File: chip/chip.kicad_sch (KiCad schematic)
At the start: 2 parts, among them J1 DF40TC-30DP-0.4V(51), U1 HOME_VFBGA67_INTERFACE

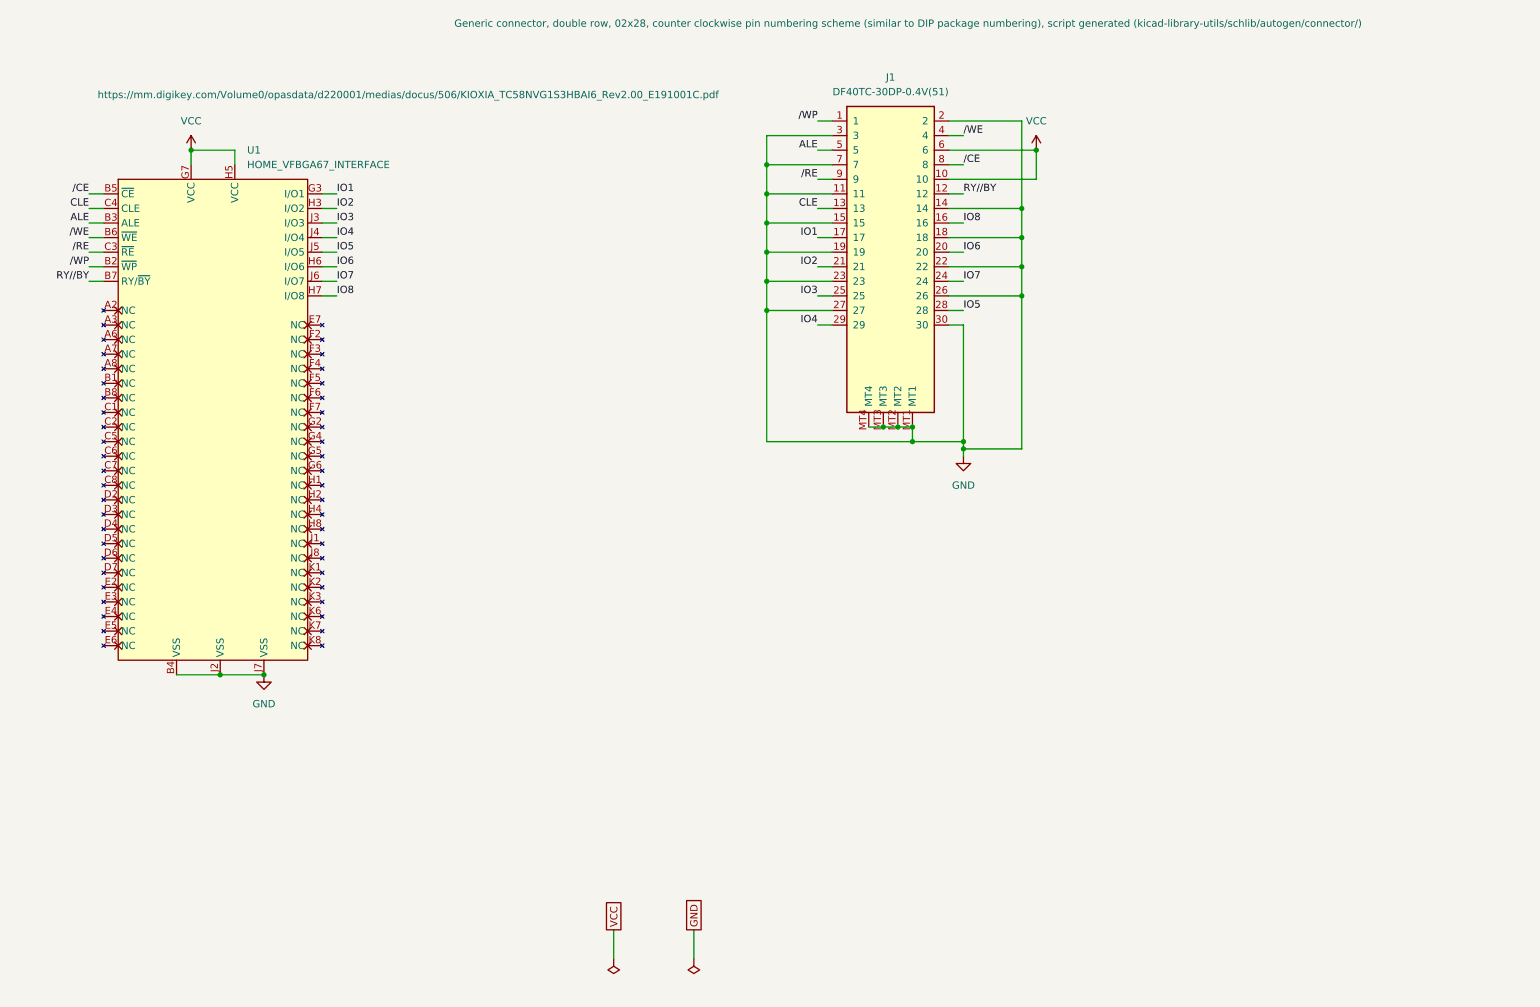
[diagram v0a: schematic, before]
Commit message: Draw board C's schematic: real NAND, DF40 receptacle, decoupling
U1 keeps the TC58NVG1S3HBAI6 symbol and every net label, but takes the
non-mirrored BGA-67 footprint and its real part number as Value. J1 swaps the
DF40 plug symbol for the 4.0 mm receptacle.

The swap is safe because the two symbols are pin-identical: 30 pins, same
numbers, same positions, same orientations, verified before the edit. So every
wire endpoint stays on the same pin number and no net moves. The plug/receptacle
difference lives entirely in the footprint, which is where the face-to-face
mirror belongs.

Adds C1 100nF and C2 1uF across VCC/GND. The target board's decoupling is now
two boards and a mated connector away from the die.

ERC clean. check_mating confirms board C's ball-to-net map is still identical
to carrier A's.

Co-Authored-By: Claude Opus 5 <noreply@anthropic.com>
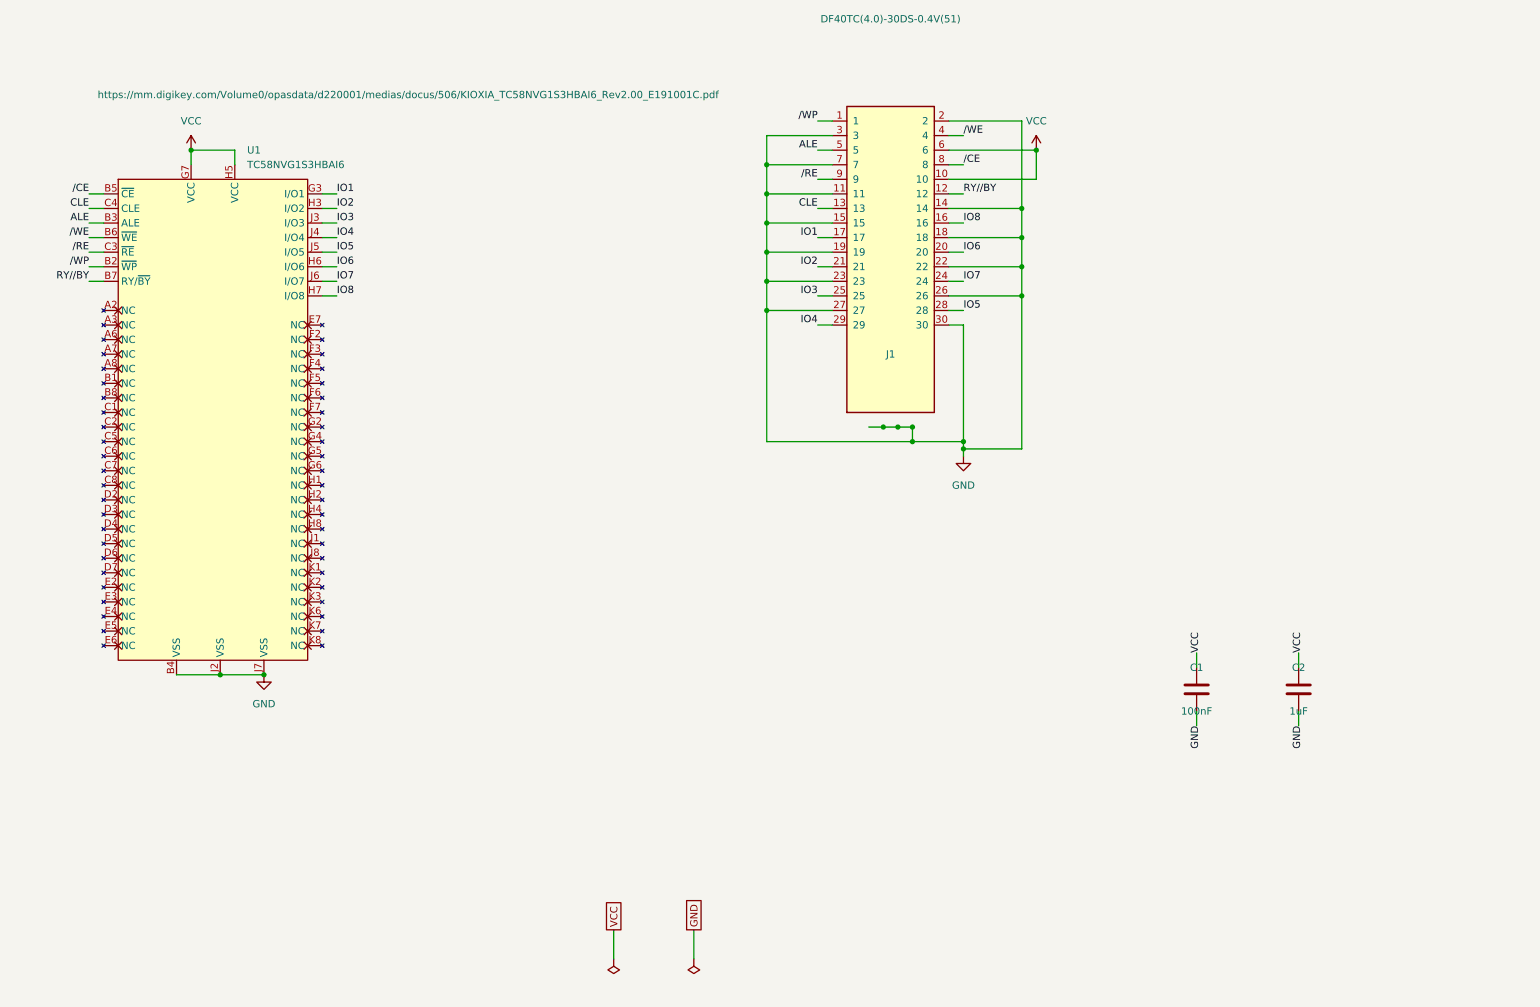
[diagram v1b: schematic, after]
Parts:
- removed J1: DF40TC-30DP-0.4V(51), Connector_Hirose_DF40:HIROSE_DF40TC-30DP-0.4V_51_, symbol carrier:DF40TC-30DP-0.4V_51_
- added C1: 100nF, Capacitor_SMD:C_0402_1005Metric, symbol Device:C
- added C2: 1uF, Capacitor_SMD:C_0402_1005Metric, symbol Device:C
- added J1: DF40TC(4.0)-30DS-0.4V(51), Connector_Hirose_DF40:HIROSE_DF40TC_4.0_-30DS-0.4V_51_, symbol carrier:DF40TC_4.0_-30DS-0.4V_51_
- U1: value HOME_VFBGA67_INTERFACE -> TC58NVG1S3HBAI6; footprint carrier:BGA-67_6.5x8.0mm_Layout8x10_P0.8mm_Mirrored_Interposer -> carrier:BGA-67_6.5x8.0mm_Layout8x10_P0.8mm
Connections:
- net ALE: now also J1.5
- net CLE: now also J1.13
- net GND: now also C1.2, C2.2, J1.11, J1.14, J1.15, J1.18, J1.19, J1.2, J1.22, J1.23, J1.26, J1.27, J1.3, J1.30, J1.7
- net IO1: now also J1.17
- net IO2: now also J1.21
- net IO3: now also J1.25
- net IO4: now also J1.29
- net IO5: now also J1.28
- net IO6: now also J1.20
- net IO7: now also J1.24
- net IO8: now also J1.16
- net RY//BY: now also J1.12
- net VCC: now also C1.1, C2.1, J1.10, J1.6
- net /CE: now also J1.8
- net /RE: now also J1.9
- net /WE: now also J1.4
- net /WP: now also J1.1

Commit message: WIP: board C routing, 5 via-in-pad violations outstanding
All 22 nets now have copper and the GND pour is filled; DRC is down to one
unconnected item, an isolated island of the pour at (164.36, 88.79).

Not fabricable yet. check_chip fails: five vias sit inside BGA pads, which
the design forbids because it would require VIPPO rather than JLC's standard
4-layer flow.

  /CLE        ball C4   0.000 mm
  /IO4        ball J4   0.000 mm
  /IO5        ball J5   0.000 mm
  VCC         ball H5   0.001 mm
  /WP         ball B2   0.005 mm

Six vias also use a 0.25 mm drill rather than the 0.20 mm the other boards
use. Legal but inconsistent.

Snapshot of the on-disk file at 02:48 with KiCad still open, so any unsaved
edits are not included.

Co-Authored-By: Claude Opus 5 <noreply@anthropic.com>
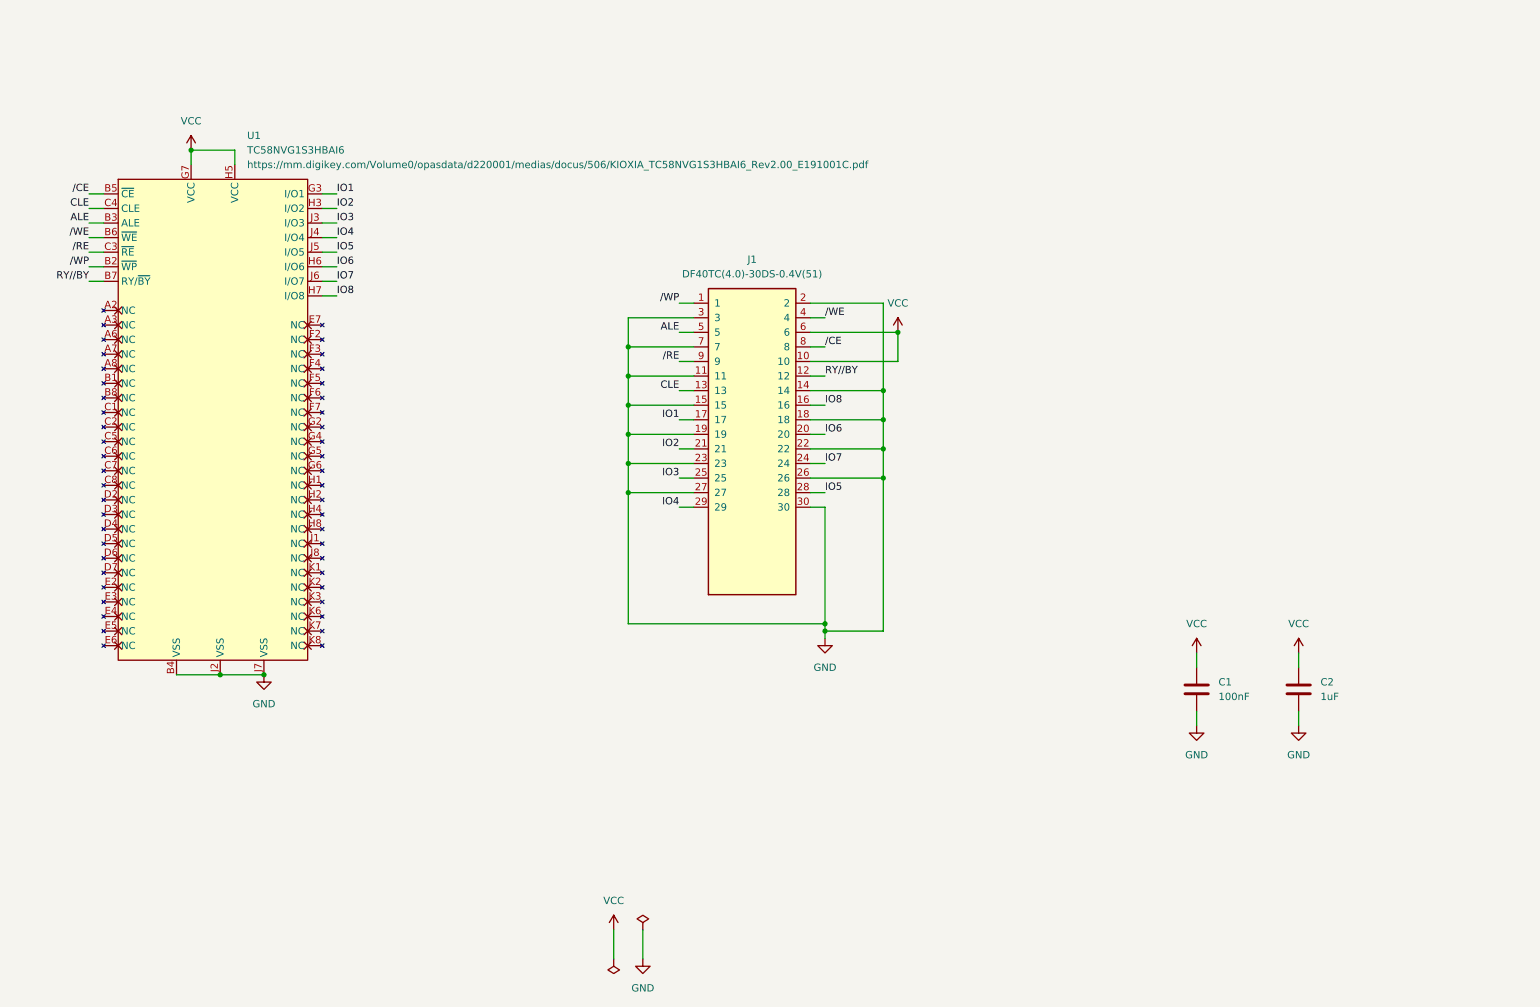
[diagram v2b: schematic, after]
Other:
- moved on the sheet: J1
